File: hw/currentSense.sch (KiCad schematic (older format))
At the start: 2 parts, among them U501 ZXCT1086

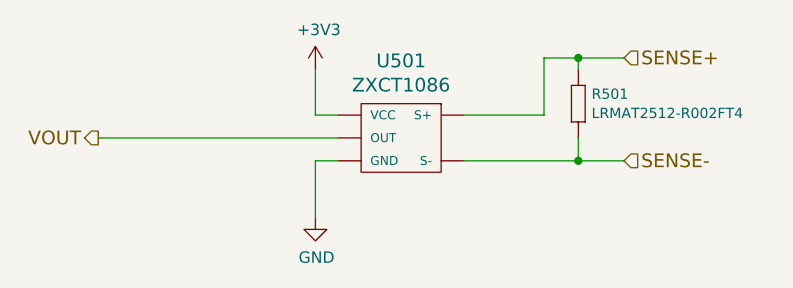
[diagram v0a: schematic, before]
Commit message: at least shortcirucuit protection works
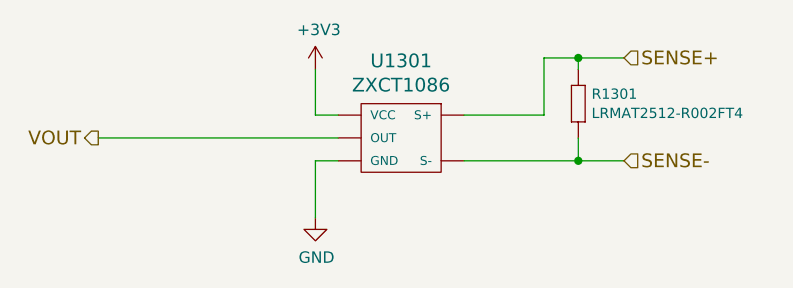
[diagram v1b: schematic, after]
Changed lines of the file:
@@
 AR Path="/5954FB0E/595CED51/594D8B7D" Ref="U1201"  Part="1"
 AR Path="/5954FB0E/59847685/594D8B7D" Ref="U1301"  Part="1"
-F 0 "U501" H 5425 3887 60  0000 C CNN
+F 0 "U1301" H 5425 3887 60  0000 C CNN
 F 1 "ZXCT1086" H 5425 3781 60  0000 C CNN
 F 2 "usevolt:SOT-25" H 5100 4050 60  0001 C CNN
@@
 $EndComp
 $Comp
-L GND #PWR016
+L GND #PWR402
 U 1 1 594D8B7E
 P 5050 4000
-AR Path="/59542AAB/595CED4D/594D8B7E" Ref="#PWR016"  Part="1"
-AR Path="/59542AAB/58BE8E7A/594D8B7E" Ref="#PWR018"  Part="1"
-AR Path="/59542AAB/58BE8E88/594D8B7E" Ref="#PWR020"  Part="1"
-AR Path="/59542AAB/58BE8E96/594D8B7E" Ref="#PWR022"  Part="1"
-AR Path="/5954FB0E/58BE8E4D/594D8B7E" Ref="#PWR027"  Part="1"
-AR Path="/5954FB0E/595CED50/594D8B7E" Ref="#PWR029"  Part="1"
-AR Path="/5954FB0E/595CED51/594D8B7E" Ref="#PWR031"  Part="1"
-AR Path="/5954FB0E/59847685/594D8B7E" Ref="#PWR033"  Part="1"
-F 0 "#PWR033" H 5050 3750 50  0001 C CNN
+AR Path="/59542AAB/595CED4D/594D8B7E" Ref="#PWR402"  Part="1"
+AR Path="/59542AAB/58BE8E7A/594D8B7E" Ref="#PWR502"  Part="1"
+AR Path="/59542AAB/58BE8E88/594D8B7E" Ref="#PWR602"  Part="1"
+AR Path="/59542AAB/58BE8E96/594D8B7E" Ref="#PWR702"  Part="1"
+AR Path="/5954FB0E/58BE8E4D/594D8B7E" Ref="#PWR902"  Part="1"
+AR Path="/5954FB0E/595CED50/594D8B7E" Ref="#PWR1002"  Part="1"
+AR Path="/5954FB0E/595CED51/594D8B7E" Ref="#PWR1102"  Part="1"
+AR Path="/5954FB0E/59847685/594D8B7E" Ref="#PWR1202"  Part="1"
+F 0 "#PWR1202" H 5050 3750 50  0001 C CNN
 F 1 "GND" H 5055 3827 50  0000 C CNN
 F 2 "" H 5050 4000 50  0000 C CNN
@@
 $EndComp
 $Comp
-L +3V3 #PWR017
+L +3V3 #PWR401
 U 1 1 589841AE
 P 5050 3350
-AR Path="/59542AAB/595CED4D/589841AE" Ref="#PWR017"  Part="1"
-AR Path="/59542AAB/58BE8E7A/589841AE" Ref="#PWR019"  Part="1"
-AR Path="/59542AAB/58BE8E88/589841AE" Ref="#PWR021"  Part="1"
-AR Path="/59542AAB/58BE8E96/589841AE" Ref="#PWR023"  Part="1"
-AR Path="/5954FB0E/58BE8E4D/589841AE" Ref="#PWR028"  Part="1"
-AR Path="/5954FB0E/595CED50/589841AE" Ref="#PWR030"  Part="1"
-AR Path="/5954FB0E/595CED51/589841AE" Ref="#PWR032"  Part="1"
-AR Path="/5954FB0E/59847685/589841AE" Ref="#PWR034"  Part="1"
-F 0 "#PWR034" H 5050 3200 50  0001 C CNN
+AR Path="/59542AAB/595CED4D/589841AE" Ref="#PWR401"  Part="1"
+AR Path="/59542AAB/58BE8E7A/589841AE" Ref="#PWR501"  Part="1"
+AR Path="/59542AAB/58BE8E88/589841AE" Ref="#PWR601"  Part="1"
+AR Path="/59542AAB/58BE8E96/589841AE" Ref="#PWR701"  Part="1"
+AR Path="/5954FB0E/58BE8E4D/589841AE" Ref="#PWR901"  Part="1"
+AR Path="/5954FB0E/595CED50/589841AE" Ref="#PWR1001"  Part="1"
+AR Path="/5954FB0E/595CED51/589841AE" Ref="#PWR1101"  Part="1"
+AR Path="/5954FB0E/59847685/589841AE" Ref="#PWR1201"  Part="1"
+F 0 "#PWR1201" H 5050 3200 50  0001 C CNN
 F 1 "+3V3" H 5065 3523 50  0000 C CNN
 F 2 "" H 5050 3350 50  0000 C CNN
@@
 AR Path="/5954FB0E/595CED51/589858BC" Ref="R1201"  Part="1"
 AR Path="/5954FB0E/59847685/589858BC" Ref="R1301"  Part="1"
-F 0 "R501" V 6208 3508 45  0000 L CNN
+F 0 "R1301" V 6208 3508 45  0000 L CNN
 F 1 "LRMAT2512-R002FT4" V 6292 3508 45  0000 L CNN
 F 2 "usevolt:2512" H 6230 3600 20  0001 C CNN

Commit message: starting to draw version 4.0.0
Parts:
- renumbered R601 to R901, U501 to U901
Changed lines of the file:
@@
 $EndDescr
 $Comp
-L ZXCT1086 U501
+L ZXCT1086 U901
 U 1 1 594D8B7D
 P 5450 3600
-AR Path="/59542AAB/595CED4D/594D8B7D" Ref="U501"  Part="1"
-AR Path="/59542AAB/58BE8E7A/594D8B7D" Ref="U601"  Part="1"
-AR Path="/59542AAB/58BE8E88/594D8B7D" Ref="U701"  Part="1"
-AR Path="/59542AAB/58BE8E96/594D8B7D" Ref="U801"  Part="1"
-AR Path="/5954FB0E/58BE8E4D/594D8B7D" Ref="U1001"  Part="1"
-AR Path="/5954FB0E/595CED50/594D8B7D" Ref="U1101"  Part="1"
-AR Path="/5954FB0E/595CED51/594D8B7D" Ref="U1201"  Part="1"
-AR Path="/5954FB0E/59847685/594D8B7D" Ref="U1301"  Part="1"
-F 0 "U1301" H 5425 3887 60  0000 C CNN
+AR Path="/5954FB0E/58BE8E4D/594D8B7D" Ref="U901"  Part="1"
+AR Path="/5954FB0E/595CED50/594D8B7D" Ref="U1001"  Part="1"
+AR Path="/5954FB0E/595CED51/594D8B7D" Ref="U1101"  Part="1"
+F 0 "U1001" H 5425 3887 60  0000 C CNN
 F 1 "ZXCT1086" H 5425 3781 60  0000 C CNN
 F 2 "usevolt:SOT-25" H 5100 4050 60  0001 C CNN
@@
 $EndComp
 $Comp
-L GND #PWR402
+L GND #PWR902
 U 1 1 594D8B7E
 P 5050 4000
-AR Path="/59542AAB/595CED4D/594D8B7E" Ref="#PWR402"  Part="1"
-AR Path="/59542AAB/58BE8E7A/594D8B7E" Ref="#PWR502"  Part="1"
-AR Path="/59542AAB/58BE8E88/594D8B7E" Ref="#PWR602"  Part="1"
-AR Path="/59542AAB/58BE8E96/594D8B7E" Ref="#PWR702"  Part="1"
 AR Path="/5954FB0E/58BE8E4D/594D8B7E" Ref="#PWR902"  Part="1"
 AR Path="/5954FB0E/595CED50/594D8B7E" Ref="#PWR1002"  Part="1"
 AR Path="/5954FB0E/595CED51/594D8B7E" Ref="#PWR1102"  Part="1"
-AR Path="/5954FB0E/59847685/594D8B7E" Ref="#PWR1202"  Part="1"
-F 0 "#PWR1202" H 5050 3750 50  0001 C CNN
+F 0 "#PWR1002" H 5050 3750 50  0001 C CNN
 F 1 "GND" H 5055 3827 50  0000 C CNN
 F 2 "" H 5050 4000 50  0000 C CNN
@@
 $EndComp
 $Comp
-L +3V3 #PWR401
+L +3V3 #PWR901
 U 1 1 589841AE
 P 5050 3350
-AR Path="/59542AAB/595CED4D/589841AE" Ref="#PWR401"  Part="1"
-AR Path="/59542AAB/58BE8E7A/589841AE" Ref="#PWR501"  Part="1"
-AR Path="/59542AAB/58BE8E88/589841AE" Ref="#PWR601"  Part="1"
-AR Path="/59542AAB/58BE8E96/589841AE" Ref="#PWR701"  Part="1"
 AR Path="/5954FB0E/58BE8E4D/589841AE" Ref="#PWR901"  Part="1"
 AR Path="/5954FB0E/595CED50/589841AE" Ref="#PWR1001"  Part="1"
 AR Path="/5954FB0E/595CED51/589841AE" Ref="#PWR1101"  Part="1"
-AR Path="/5954FB0E/59847685/589841AE" Ref="#PWR1201"  Part="1"
-F 0 "#PWR1201" H 5050 3200 50  0001 C CNN
+F 0 "#PWR1001" H 5050 3200 50  0001 C CNN
 F 1 "+3V3" H 5065 3523 50  0000 C CNN
 F 2 "" H 5050 3350 50  0000 C CNN
@@
 AR Path="/58C7B0A8/594D8B83/589858BC" Ref="R?"  Part="1"
 AR Path="/59542AAB/58BE8E4D/589858BC" Ref="R?"  Part="1"
-AR Path="/59542AAB/58BE8E7A/589858BC" Ref="R601"  Part="1"
-AR Path="/59542AAB/58BE8E88/589858BC" Ref="R701"  Part="1"
-AR Path="/59542AAB/58BE8E96/589858BC" Ref="R801"  Part="1"
-AR Path="/5954FB0E/58BE8E4D/589858BC" Ref="R1001"  Part="1"
+AR Path="/59542AAB/58BE8E7A/589858BC" Ref="R?"  Part="1"
+AR Path="/59542AAB/58BE8E88/589858BC" Ref="R?"  Part="1"
+AR Path="/59542AAB/58BE8E96/589858BC" Ref="R?"  Part="1"
+AR Path="/5954FB0E/58BE8E4D/589858BC" Ref="R901"  Part="1"
 AR Path="/5954FB0E/58BE8E7A/589858BC" Ref="R?"  Part="1"
 AR Path="/5954FB0E/58BE8E88/589858BC" Ref="R?"  Part="1"
-AR Path="/59542AAB/595CED4D/589858BC" Ref="R501"  Part="1"
-AR Path="/5954FB0E/595CED50/589858BC" Ref="R1101"  Part="1"
-AR Path="/5954FB0E/595CED51/589858BC" Ref="R1201"  Part="1"
-AR Path="/5954FB0E/59847685/589858BC" Ref="R1301"  Part="1"
-F 0 "R1301" V 6208 3508 45  0000 L CNN
+AR Path="/59542AAB/595CED4D/589858BC" Ref="R?"  Part="1"
+AR Path="/5954FB0E/595CED50/589858BC" Ref="R1001"  Part="1"
+AR Path="/5954FB0E/595CED51/589858BC" Ref="R1101"  Part="1"
+AR Path="/5954FB0E/59847685/589858BC" Ref="R?"  Part="1"
+F 0 "R1001" V 6208 3508 45  0000 L CNN
 F 1 "LRMAT2512-R002FT4" V 6292 3508 45  0000 L CNN
 F 2 "usevolt:2512" H 6230 3600 20  0001 C CNN
